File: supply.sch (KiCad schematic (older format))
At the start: 76 parts, among them IC1 TPS54561, J3 DC_SOCKET, U10 LM3881MME_NOPB, U2 TPS65295RJET

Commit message: Add I2C connector
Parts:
- removed C100: C_10n_0603, rdimm-breakout-footprints:0603-cap, symbol rdimm-breakout:C_10n_0603-rdimm-breakout
- removed C101: C_100n_0402_6V3, rdimm-breakout-footprints:0402-cap, symbol rdimm-breakout:C_100n_0402_6V3-antmicroCapacitors0402-rdimm-breakout
- removed R55: R_0R_0402, rdimm-breakout-footprints:0402-res, symbol rdimm-breakout:R_0R_0402-rdimm-breakout
- removed R88: R_10k_0402, rdimm-breakout-footprints:0402-res, symbol rdimm-breakout:R_10k_0402-rdimm-breakout
- removed S1: EG1218, rdimm-breakout-footprints:Switch_Slide_11.6x4mm_EG1218, symbol rdimm-breakout:EG1218-rdimm-breakout
- removed TP6: TP_SMD1MM, rdimm-breakout-footprints:Testpoint_smd_1mm, symbol rdimm-breakout:TP_SMD1MM-rdimm-breakout
- removed U10: LM3881MME_NOPB, rdimm-breakout-footprints:VSSOP8-Texas_Instruments-DGK0008A, symbol rdimm-breakout:LM3881MME_NOPB-rdimm-breakout
- added S3: MSS3-V-T_R, rdimm-breakout-footprints:Switch_Slide_MSS3, symbol rdimm-breakout:MSS3-V-T_R
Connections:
- net labels removed: VCC_INT_EN
- wire segments 127 -> 108
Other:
- note removed: "Power sequencer"
- note removed: "STEP1 - VCCINT (1.0V) for FPGA\nSTEP2 - VCCAUX (1.8V, 2.5V, 1.2V) for FPGA and DDR\nSTEP3 - VCCIO (3.3V, 1.2V, 0.6V) for FPGA, PHY and DDR"
- moved on the sheet: 0V6, 12V1, 1V2, 2V5, 5V0, TP7, TP8

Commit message: Add FTDI and USB power supply
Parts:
- removed 0V6, 1V2, TP7, TP8, TP9: TP_SMD1MM, rdimm-breakout-footprints:Testpoint_smd_1mm, symbol rdimm-breakout:TP_SMD1MM-rdimm-breakout
- removed C1, C33: C_10u_0603, rdimm-breakout-footprints:0603-cap, symbol rdimm-breakout:C_10u_0603-rdimm-breakout
- removed C106, C107, C108, C109, C110, C111, C112, C113: C_10n_0603, rdimm-breakout-footprints:0603-cap, symbol rdimm-breakout:C_10n_0603-rdimm-breakout
- removed C116, C117, C118: C_47u_16V_1206, rdimm-breakout-footprints:1206-cap, symbol rdimm-breakout:C_47u_16V_1206-rdimm-breakout
- removed C159, C31, C39, C40, C41, C42: C_22u_0603, rdimm-breakout-footprints:0603-cap, symbol rdimm-breakout:C_22u_0603-rdimm-breakout
- removed C172: C_4n7_0402, rdimm-breakout-footprints:0402-cap, symbol rdimm-breakout:C_4n7_0402-rdimm-breakout
- removed C174: C_10n_0402, rdimm-breakout-footprints:0402-cap, symbol rdimm-breakout:C_10n_0402-rdimm-breakout
- removed C175: C_47p_0402, rdimm-breakout-footprints:0402-cap, symbol rdimm-breakout:C_47p_0402-rdimm-breakout
- removed C178, C35: C_100n_0402_6V3, rdimm-breakout-footprints:0402-cap, symbol rdimm-breakout:C_100n_0402_6V3-rdimm-breakout
- removed C180, C182, C183: C_47u_0603, rdimm-breakout-footprints:0603-cap, symbol rdimm-breakout:C_47u_0603-rdimm-breakout
- removed C2: C_100n_0603, rdimm-breakout-footprints:0603-cap, symbol rdimm-breakout:C_100n_0603-rdimm-breakout
- removed C27, C28, C29: C_10u_25V_0603, rdimm-breakout-footprints:0603-cap, symbol rdimm-breakout:C_10u_25V_0603-rdimm-breakout
- removed C30: C_100n_0402_16V, rdimm-breakout-footprints:0402-cap, symbol rdimm-breakout:C_100n_0402_16V-rdimm-breakout
- removed C36: C_470n_0402, rdimm-breakout-footprints:0402-cap, symbol rdimm-breakout:C_470n_0402-rdimm-breakout
- removed C38: C_10u_0402, rdimm-breakout-footprints:0402-cap, symbol rdimm-breakout:C_10u_0402-rdimm-breakout
- removed C4: C_1u_0603, rdimm-breakout-footprints:0603-cap, symbol rdimm-breakout:C_1u_0603-rdimm-breakout
- removed D11, D2: PDS760-13, rdimm-breakout-footprints:PDS760-13, symbol rdimm-breakout:PDS760-13-rdimm-breakout
- removed F1, F2, F3: 1206L450SLWR, rdimm-breakout-footprints:1206-res, symbol rdimm-breakout:1206L450SLWR-rdimm-breakout
- removed IC1: TPS54561, rdimm-breakout-footprints:WSON-10_4x4, symbol rdimm-breakout:TPS54561-rdimm-breakout
- removed J3: DC_SOCKET, rdimm-breakout-footprints:DC_SOCKET, symbol rdimm-breakout:DC_SOCKET-rdimm-breakout
- removed L1: IHLP2020BZER4R7M01, rdimm-breakout-footprints:IHLP2020BZER4R7M01, symbol rdimm-breakout:IHLP2020BZER4R7M01-rdimm-breakout
- removed L2: DFE322512F-R68M=P2, rdimm-breakout-footprints:INDC3225X120N, symbol rdimm-breakout:DFE322512F-R68M=P2-rdimm-breakout
- removed L6: WE_7447798720, rdimm-breakout-footprints:WE_7447798720, symbol rdimm-breakout:WE_7447798720-rdimm-breakout
- removed R115: R_16k9_0402, rdimm-breakout-footprints:0402-res, symbol rdimm-breakout:R_16k9_0402-rdimm-breakout
- removed R116: R_243k_0402, rdimm-breakout-footprints:0402-res, symbol rdimm-breakout:R_243k_0402-rdimm-breakout
- removed R122, R40: R_100k_0402, rdimm-breakout-footprints:0402-res, symbol rdimm-breakout:R_100k_0402-rdimm-breakout
- removed R126: R_49R9_0402, rdimm-breakout-footprints:0402-res, symbol rdimm-breakout:R_49R9_0402-rdimm-breakout
- removed R127: R_53k6_0402, rdimm-breakout-footprints:0402-res, symbol rdimm-breakout:R_53k6_0402-rdimm-breakout
- removed R128: R_10k2_0402, rdimm-breakout-footprints:0402-res, symbol rdimm-breakout:R_10k2_0402-rdimm-breakout
- removed R159, R161: R_0R_0603, rdimm-breakout-footprints:0603-res, symbol rdimm-breakout:R_0R_0603-rdimm-breakout
- removed R35: R_5R1_0402, rdimm-breakout-footprints:0402-res, symbol rdimm-breakout:R_5R1_0402-rdimm-breakout
- removed R42: R_0R_0402, rdimm-breakout-footprints:0402-res, symbol rdimm-breakout:R_0R_0402-rdimm-breakout
- removed R86, R87: R_10k_0402, rdimm-breakout-footprints:0402-res, symbol rdimm-breakout:R_10k_0402-rdimm-breakout
- removed U2: TPS65295RJET, rdimm-breakout-footprints:TPS65295RJET, symbol rdimm-breakout:TPS65295RJET-rdimm-breakout
- added 1V8_FT: TP_SMD1MM, rdimm-breakout-footprints:Testpoint_smd_1mm, symbol rdimm-breakout:TP_SMD1MM-rdimm-breakout
- added C? (x4): C_1u_0402, rdimm-breakout-footprints:0402-cap, symbol rdimm-breakout:C_1u_0402
- added C? (x2): C_27p_0402, rdimm-breakout-footprints:0402-cap, symbol rdimm-breakout:C_27p_0402
- added C? (x12): C_100n_0402, rdimm-breakout-footprints:0402-cap, symbol rdimm-breakout:C_100n_0402
- added C? (x3): C_4u7_0402, rdimm-breakout-footprints:0402-cap, symbol rdimm-breakout:C_4u7_0402
- added D?: PESD5V0S2BQA, rdimm-breakout-footprints:TPD2E009DRTR, symbol rdimm-breakout:PESD5V0S2BQA
- added FB? (x3): BLM18AG601SN1D, rdimm-breakout-footprints:0603, symbol rdimm-breakout:BLM18AG601SN1D
- added IC?: MIC5225-3.3YM5-TR, rdimm-breakout-footprints:SOT-23-5, symbol rdimm-breakout:TPS7A0518PDBVT
- added IC?: MIC5317-2.5YM5-TR, rdimm-breakout-footprints:SOT-23-5, symbol rdimm-breakout:TPS7A0518PDBVT
- added J?: WE_629105150521, rdimm-breakout-footprints:USB_Micro_B_Female_629105150521, symbol rdimm-breakout:WE_629105150521
- added R? (x3): R_0R_0603, rdimm-breakout-footprints:0603-res, symbol rdimm-breakout:R_0R_0603
- added R?: R_12k_0402, rdimm-breakout-footprints:0402-res, symbol rdimm-breakout:R_12k_0402
- added R?: R_4k7_0402, rdimm-breakout-footprints:0402-res, symbol rdimm-breakout:R_4k7_0402
- added R?: R_10k_0402, rdimm-breakout-footprints:0402-res, symbol rdimm-breakout:R_10k_0402
- added R?: R_220R_0402, rdimm-breakout-footprints:0402-res, symbol rdimm-breakout:R_220R_0402
- added U?: FT2232HL-REEL, rdimm-breakout-footprints:LQFP-64_10x10mm, symbol rdimm-breakout:FT2232HL-REEL
- added Y?: KX-7_12,MHz, rdimm-breakout-footprints:KX-7, symbol rdimm-breakout:KX-7_12,MHz
- renumbered 12V1 to 3V3
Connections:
- net labels added: 1V8_FT, 3V3_EN, 5V_USB, FTDI_RST, OSCI, OSCO, SCL, SDA, USB_D_N, USB_D_P, VBUS, WP
- net labels removed: 3V3_SYS, 5V0_SYS, SYS_EN, SYS_ON, VCC0V6, VCC5V0_INT, VCC_AUX_EN, VCC_IO_EN, VDD1V2, VDDQ, VIN, VLDOIN, VPP, VTT, VTTREF
- wire segments 108 -> 102
- no-connect marks 0 -> 5
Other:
- note added: "2V5 LDO"
- note added: "3V3 LDO"
- note added: "FTDI"
- note added: "Power LED"
- note added: "Power filltering"
- note added: "USB connector"
- note removed: "DDR4"
- note removed: "DDR4 PMIC"
- note removed: "Filtering"
- note removed: "Input"
- note removed: "Input power connector"
- note removed: "Main supply (5V 5A)"
- note removed: "Output"
- note removed: "Plane Decoupling"
- note removed: "Shunt resistors"
- note removed: "VCC5V0 4.5V to 5.5V"
- note removed: "VDDQ 1.2V 8A"
- note removed: "VIN 4.5V to 18V"
- note removed: "VPP 2.5V 1A"
- note removed: "VTT 0.6V 1A"
- moved on the sheet: 2V5, 3V3, 5V0, PWR1, R119, S3

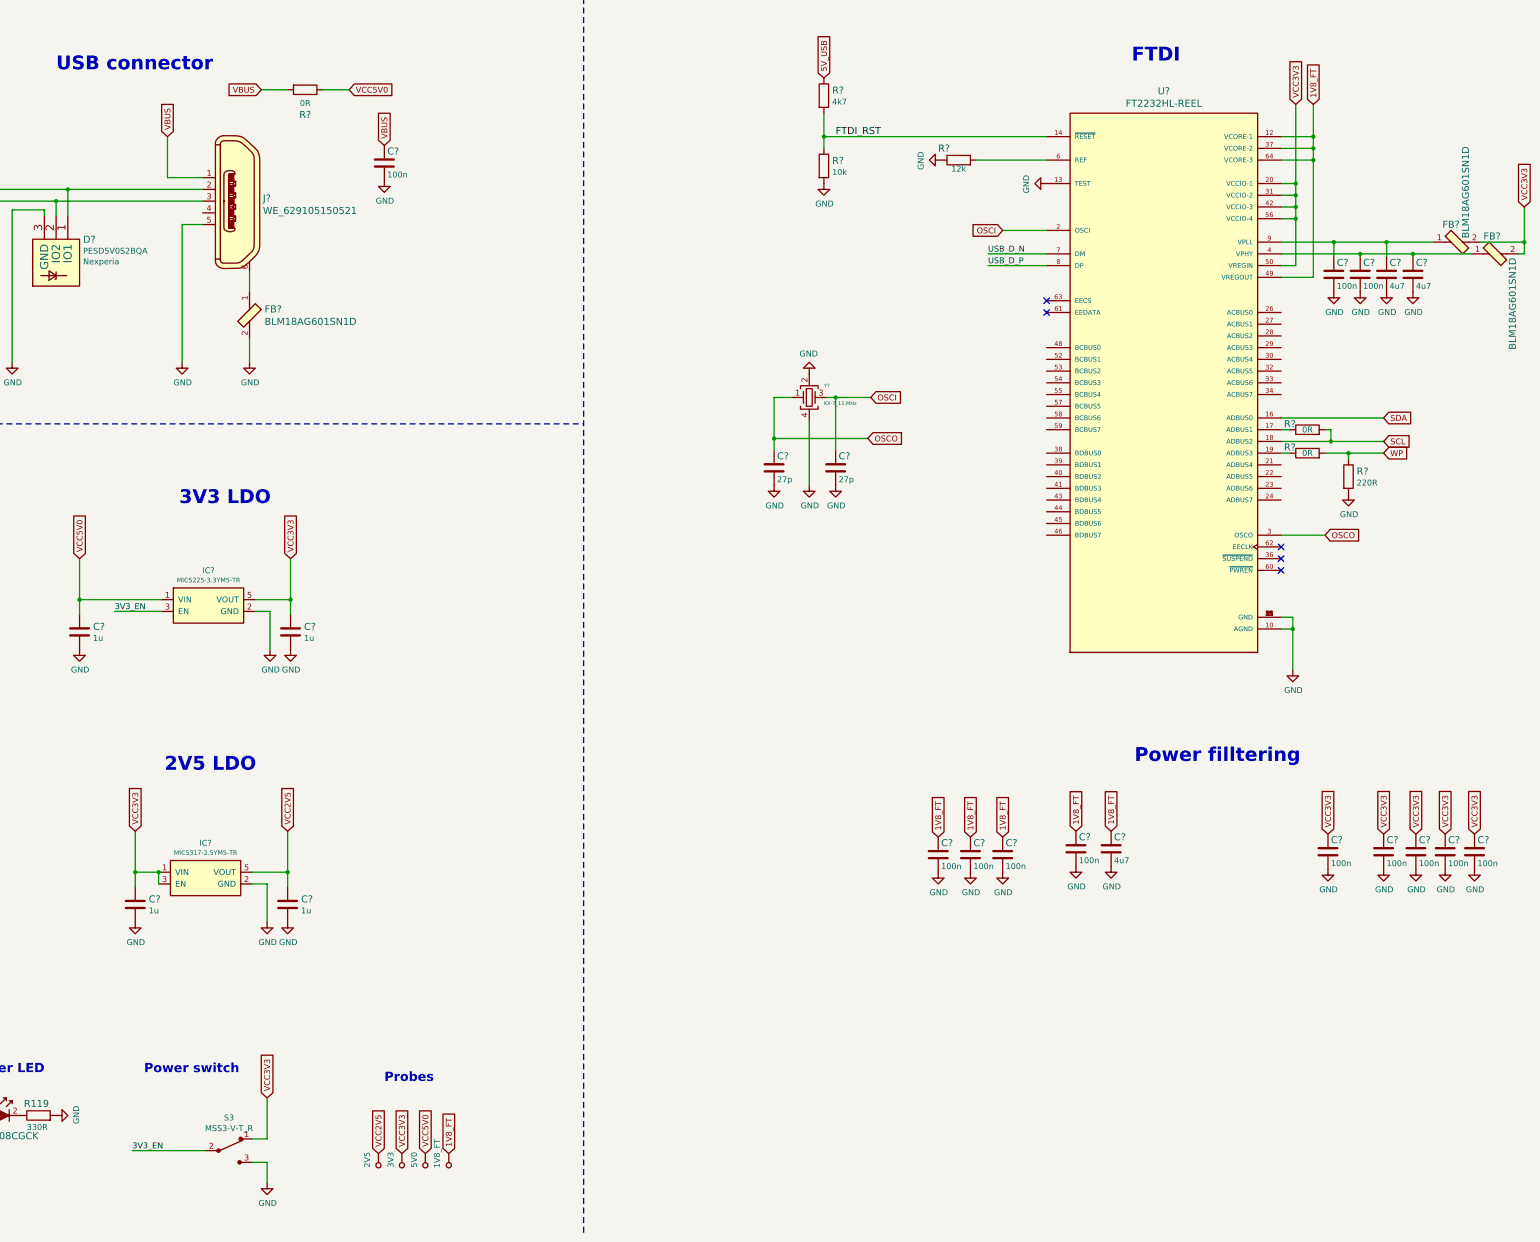
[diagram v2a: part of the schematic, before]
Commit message: Update labels on the schematics
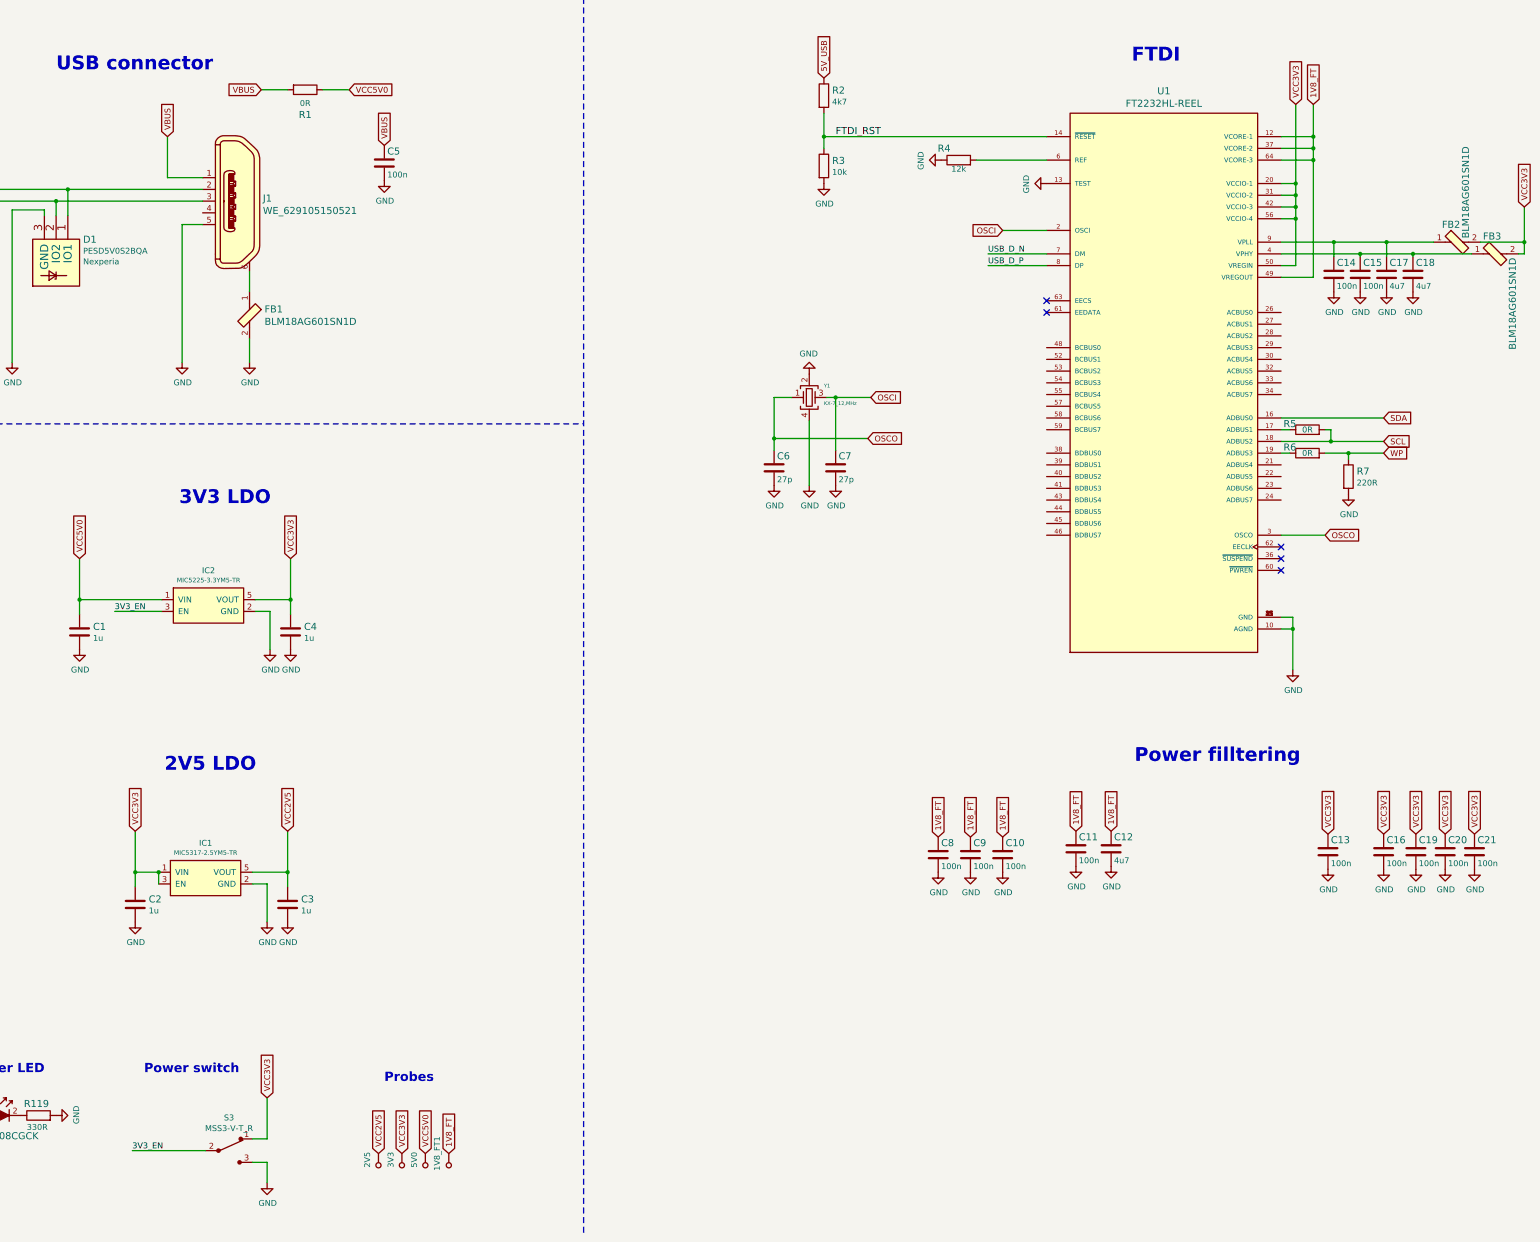
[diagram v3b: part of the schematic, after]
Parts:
- removed U?: FT2232HL-REEL, rdimm-breakout-footprints:LQFP-64_10x10mm, symbol rdimm-breakout:FT2232HL-REEL
- added U1: FT2232HL-REEL, rdimm-breakout-footprints:LQFP-64_10x10mm, symbol rdimm-breakout:FT2232HL-REEL
- gave numbers to parts that had none: 36
- renumbered 1V8_FT to 1V8_FT1
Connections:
- net 1V8_FT: now also U1.12 (VCORE-1), U1.37 (VCORE-2), U1.49 (VREGOUT), U1.64 (VCORE-3)
- net FTDI_RST: now also U1.14 (~RESET)
- net GND: now also U1.1 (GND), U1.10 (AGND), U1.11 (GND), U1.13 (TEST), U1.15 (GND), U1.25 (GND), U1.35 (GND), U1.47 (GND), U1.5 (GND), U1.51 (GND)
- net OSCI: now also U1.2 (OSCI)
- net OSCO: now also U1.3 (OSCO)
- net SCL: now also U1.18 (ADBUS2)
- net SDA: now also U1.16 (ADBUS0)
- net USB_D_N: now also U1.7 (DM)
- net USB_D_P: now also U1.8 (DP)
- net VCC3V3: now also U1.20 (VCCIO-1), U1.31 (VCCIO-2), U1.42 (VCCIO-3), U1.50 (VREGIN), U1.56 (VCCIO-4)
- net at R4.2: now also U1.6 (REF)
- net at R5.1: now also U1.17 (ADBUS1)
- net at R6.1: now also U1.19 (ADBUS3)
- net at C15.1, C18.1, FB3.1: now also U1.4 (VPHY)
- net at C14.1, C17.1, FB2.1: now also U1.9 (VPLL)

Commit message: Add initial component placement
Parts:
- U1: footprint rdimm-breakout-footprints:LQFP-64_10x10mm -> antmicro-footprints:LQFP-64_10x10mm; symbol rdimm-breakout:FT2232HL-REEL -> antmicroInterfaceControllers:FT2232HL-REEL
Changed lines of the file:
@@
 	12250 4275 13125 4275
 $Comp
-L rdimm-breakout:FT2232HL-REEL U1
+L antmicroInterfaceControllers:FT2232HL-REEL U1
 U 1 1 624D5D0F
 P 11250 3975
 F 0 "U1" H 11250 6464 60  0000 C CNN
 F 1 "FT2232HL-REEL" H 11250 6358 60  0000 C CNN
-F 2 "rdimm-breakout-footprints:LQFP-64_10x10mm" V 11300 4200 60  0001 L CNN
+F 2 "antmicro-footprints:LQFP-64_10x10mm" V 11300 4200 60  0001 L CNN
 F 3 "https://www.ftdichip.com/Support/Documents/DataSheets/ICs/DS_FT2232H.pdf" H 7525 4000 60  0001 L CNN
 F 4 "FTDI, Future Technology Devices International Ltd" H 7525 4800 60  0001 L CNN "Manufacturer"

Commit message: Add layout
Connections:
- net labels removed: 5V_USB
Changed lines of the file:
@@
 Wire Wire Line
 	8350 1875 8350 1675
-Text GLabel 8350 1375 1    50   Input ~ 0
-5V_USB
 Wire Wire Line
 	8350 1875 10250 1875
@@
 	1    0    0    -1
 $EndComp
+Text GLabel 8350 1375 1    50   Input ~ 0
+VCC3V3
 $EndSCHEMATC

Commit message: Replace LDO
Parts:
- removed IC2: MIC5225-3.3YM5-TR, rdimm-breakout-footprints:SOT-23-5, symbol rdimm-breakout:TPS7A0518PDBVT
- added U?: NCP163ASN330T1G, antmicro-footprints:SOT-23-5, symbol antmicroPMICVoltageRegulatorsLinear:NCP163ASN330T1G
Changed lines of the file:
@@
 Wire Wire Line
 	2000 5825 2700 5825
-$Comp
-L rdimm-breakout:TPS7A0518PDBVT IC2
-U 1 1 62044E66
-P 3100 5875
-F 0 "IC2" H 3100 6174 50  0000 C CNN
-F 1 "MIC5225-3.3YM5-TR" H 3100 6091 39  0000 C CNN
-F 2 "rdimm-breakout-footprints:SOT-23-5" H 3100 5625 50  0001 C CNN
-F 3 "" H 3100 5875 50  0001 C CNN
-F 4 "MIC5225-3.3YM5-TR" H 3100 6190 50  0001 C CNN "MPN"
-F 5 "MICROCHIP" H 3100 6099 50  0001 C CNN "Manufacturer"
-	1    3100 5875
-	1    0    0    -1
-$EndComp
 Wire Wire Line
 	2300 5925 2700 5925
@@
 Text GLabel 8350 1375 1    50   Input ~ 0
 VCC3V3
+$Comp
+L antmicroPMICVoltageRegulatorsLinear:NCP163ASN330T1G U?
+U 1 1 617E4A9E
+P 3100 5875
+F 0 "U?" H 3100 6174 50  0000 C CNN
+F 1 "NCP163ASN330T1G" H 3100 6091 39  0000 C CNN
+F 2 "antmicro-footprints:SOT-23-5" H 3100 5625 50  0001 C CNN
+F 3 "https://pl.mouser.com/datasheet/2/308/1/NCP163_D-2317108.pdf" H 3200 6225 50  0001 C CNN
+F 4 "NCP163ASN330T1G" H 2950 6175 50  0001 C CNN "MPN"
+F 5 "Onsemi" H 3050 6275 50  0001 C CNN "Manufacturer"
+	1    3100 5875
+	1    0    0    -1
+$EndComp
 $EndSCHEMATC

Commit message: Bump rev to 1.0.1
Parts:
- U1: footprint antmicro-footprints:LQFP-64_10x10mm -> rdimm-breakout-footprints:LQFP-64_10x10mm; symbol antmicroInterfaceControllers:FT2232HL-REEL -> rdimm-breakout:FT2232HL-REEL
- U?: footprint antmicro-footprints:SOT-23-5 -> rdimm-breakout-footprints:SOT-23-5; symbol antmicroPMICVoltageRegulatorsLinear:NCP163ASN330T1G -> rdimm-breakout:NCP163ASN330T1G
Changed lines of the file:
@@
 Sheet 2 4
 Title "RDIMM-breakout"
-Date "2021-09"
-Rev "1.0.0"
+Date "2021-10"
+Rev "1.0.1"
 Comp "Antmicro Ltd."
 Comment1 "www.antmicro.com"
@@
 	12250 4275 13125 4275
 $Comp
-L antmicroInterfaceControllers:FT2232HL-REEL U1
+L rdimm-breakout:FT2232HL-REEL U1
 U 1 1 624D5D0F
 P 11250 3975
 F 0 "U1" H 11250 6464 60  0000 C CNN
 F 1 "FT2232HL-REEL" H 11250 6358 60  0000 C CNN
-F 2 "antmicro-footprints:LQFP-64_10x10mm" V 11300 4200 60  0001 L CNN
+F 2 "rdimm-breakout-footprints:LQFP-64_10x10mm" V 11300 4200 60  0001 L CNN
 F 3 "https://www.ftdichip.com/Support/Documents/DataSheets/ICs/DS_FT2232H.pdf" H 7525 4000 60  0001 L CNN
 F 4 "FTDI, Future Technology Devices International Ltd" H 7525 4800 60  0001 L CNN "Manufacturer"
@@
 VCC3V3
 $Comp
-L antmicroPMICVoltageRegulatorsLinear:NCP163ASN330T1G U?
+L rdimm-breakout:NCP163ASN330T1G U?
 U 1 1 617E4A9E
 P 3100 5875
 F 0 "U?" H 3100 6174 50  0000 C CNN
 F 1 "NCP163ASN330T1G" H 3100 6091 39  0000 C CNN
-F 2 "antmicro-footprints:SOT-23-5" H 3100 5625 50  0001 C CNN
+F 2 "rdimm-breakout-footprints:SOT-23-5" H 3100 5625 50  0001 C CNN
 F 3 "https://pl.mouser.com/datasheet/2/308/1/NCP163_D-2317108.pdf" H 3200 6225 50  0001 C CNN
 F 4 "NCP163ASN330T1G" H 2950 6175 50  0001 C CNN "MPN"

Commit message: Annotate components
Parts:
- gave numbers to parts that had none: 1
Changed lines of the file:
@@
 VCC3V3
 $Comp
-L rdimm-breakout:NCP163ASN330T1G U?
+L rdimm-breakout:NCP163ASN330T1G U2
 U 1 1 617E4A9E
 P 3100 5875
-F 0 "U?" H 3100 6174 50  0000 C CNN
+F 0 "U2" H 3100 6174 50  0000 C CNN
 F 1 "NCP163ASN330T1G" H 3100 6091 39  0000 C CNN
 F 2 "rdimm-breakout-footprints:SOT-23-5" H 3100 5625 50  0001 C CNN
